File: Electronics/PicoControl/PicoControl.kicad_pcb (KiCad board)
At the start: 2 copper layers, 177.8 x 127 mm, 48 parts, among them CN1 Battery, CN2 EQ, CN3 DEC, CN4 FOCUS, CN5 Camera, J1 Conn_01x03_Pin, J2 Conn_01x03_Socket, J4 Conn_01x06_Pin, U1 TPS54360BDDAR, U2 TPS54360BDDAR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

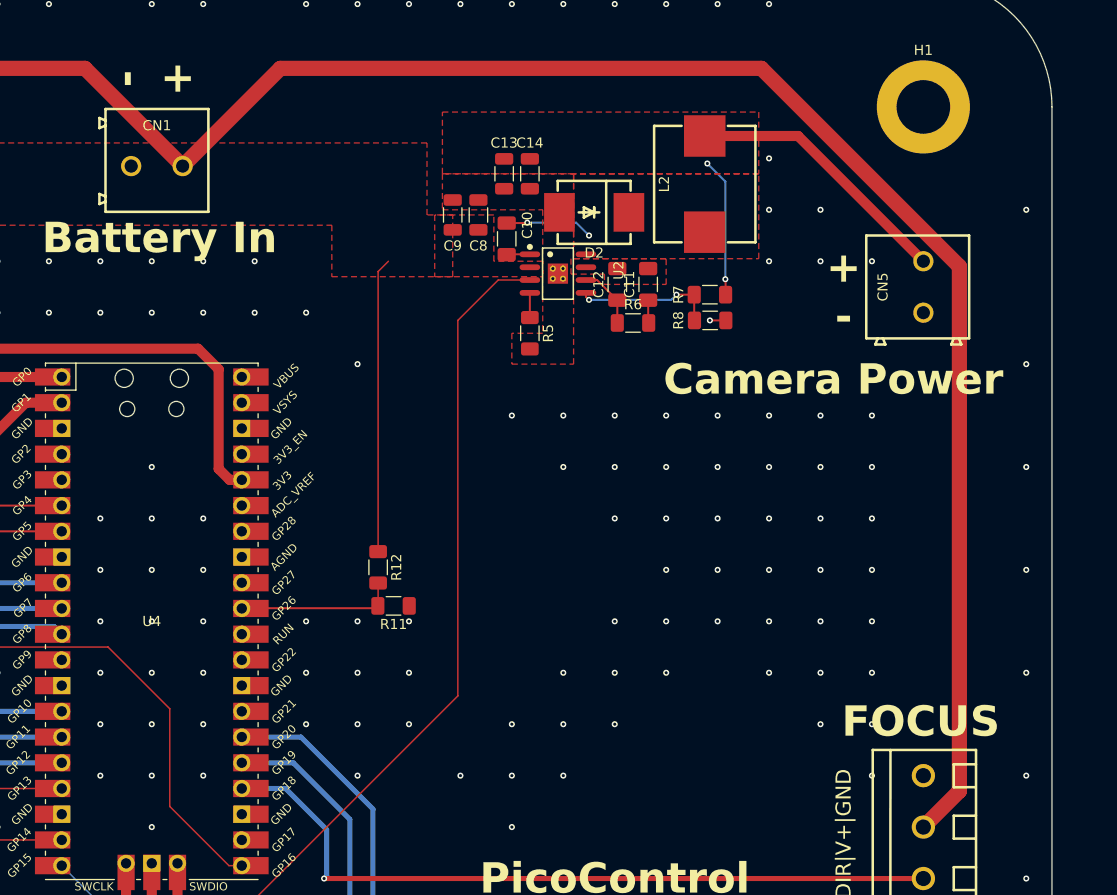
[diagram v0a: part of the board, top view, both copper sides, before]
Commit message: Updated PCB to Include Hall Sensors
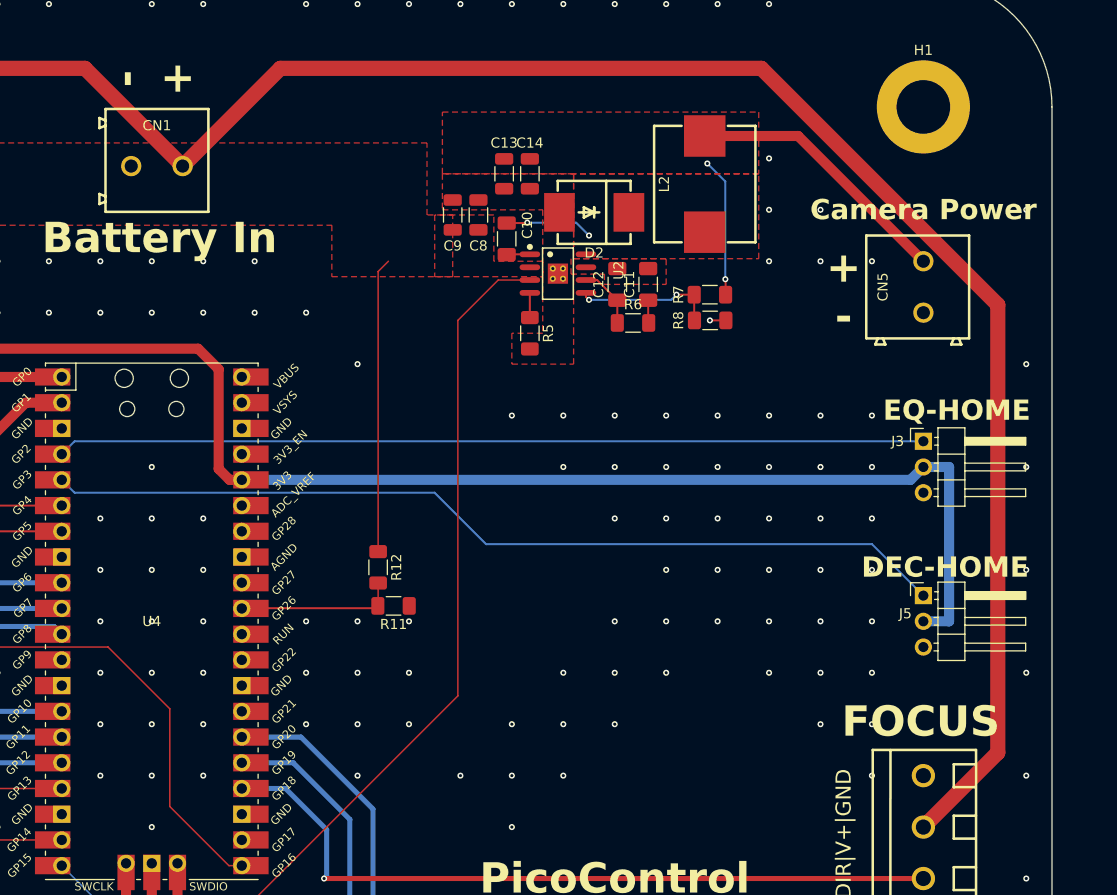
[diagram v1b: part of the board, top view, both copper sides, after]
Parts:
- added J3: Conn_01x03_Pin, Connector_PinHeader_2.54mm:PinHeader_1x03_P2.54mm_Horizontal, F.Cu at (228.6, 83.8)
- added J5: Conn_01x03_Pin, Connector_PinHeader_2.54mm:PinHeader_1x03_P2.54mm_Horizontal, F.Cu at (228.6, 99.1)
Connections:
- U4 pad 4: unconnected-(U4-GPIO2-Pad4) -> /EQ_HALL
- U4 pad 5: unconnected-(U4-GPIO3-Pad5) -> /DEC_HALL
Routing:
- net /DEC_HALL: track 0.00 -> 89.8 mm
- net +3.3V: track 101.5 -> 189.7 mm
- net /EQ_HALL: track 0.00 -> 85.6 mm
- net VCC: track 337.9 -> 341.0 mm
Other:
- board text added: "DEC-HOME"
- board text added: "EQ-HOME"
